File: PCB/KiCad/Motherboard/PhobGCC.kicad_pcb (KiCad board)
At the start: 2 copper layers, 125.5 x 72.9 mm, 67 parts, among them J1 Conn_01x06_Female, J2 Conn_01x04_Female, J3 Conn_01x01_Male, J5 Conn_01x02_Male, Q1 Q_NMOS_GSD, Q2 Q_PMOS_GDS, Q3 Q_NMOS_GSD, SW1 A, SW10 Dup, SW11 Dright, SW12 Ddown, SW2 B, SW3 X, SW4 Y, SW5 Start, SW6 L, SW7 R, SW8 1825027-5, SW9 Dleft, U1 Teensy4.0, U2 2x DRV5053CAQLPGM Hall Effect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, U3 GP2S60-MFG, U4 GP2S60-MFG

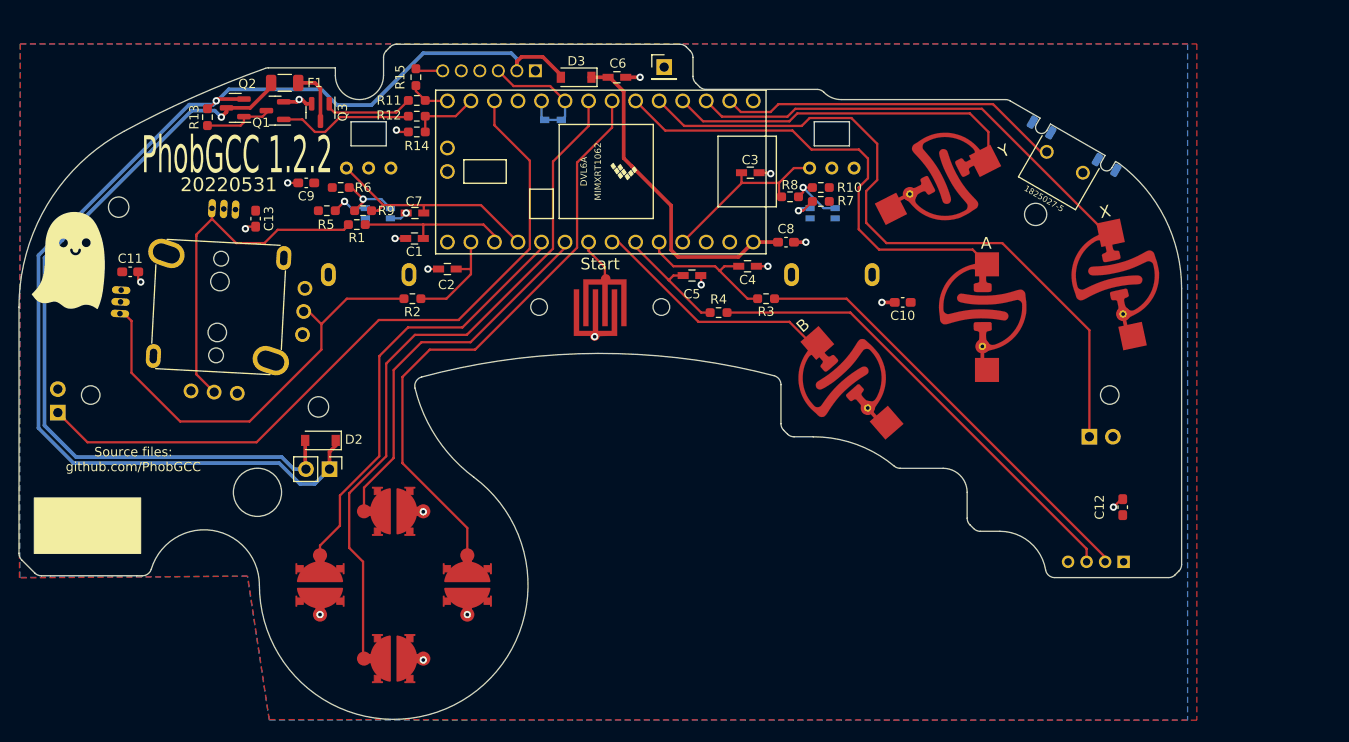
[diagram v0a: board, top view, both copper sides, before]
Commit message: Updates
- switched rumble pads to SMD and matched OEM placement.
- aligned both sets of trigger pads to be horizontal for convenience and consistency.
- centered c-stick pins to the board edge.
- rerouted some areas to have a more consistent copper fill.
- fixed trigger board width (switched 7.5mm to 7.35mm).
- increased dpad button pad size to make for easier hand soldering.
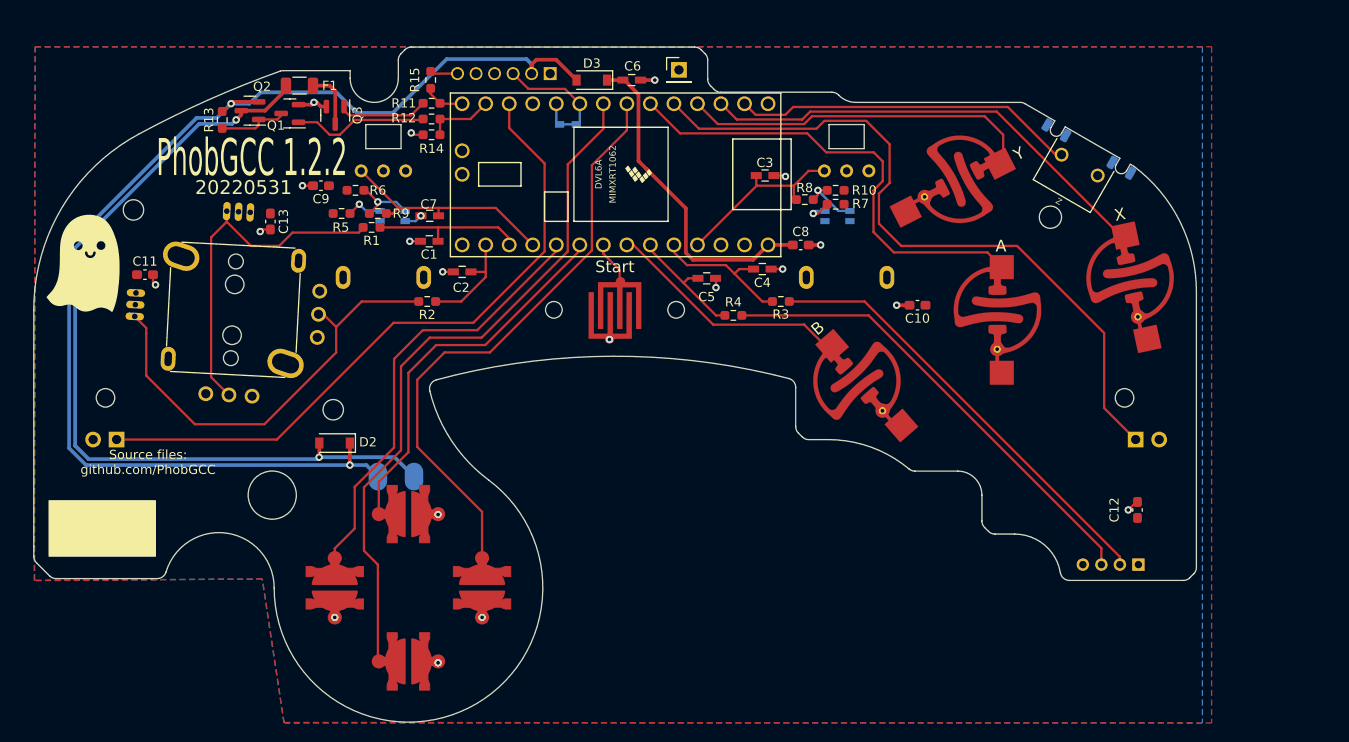
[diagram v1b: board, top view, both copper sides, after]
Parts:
- J5: moved to B.Cu
- SW8: value 1825027-5 -> Z
- moved SW6 6.98 mm to (46.5, 68.4), turned to 90 degrees
- moved J5 6.06 mm to (75.5, 72.3)
- moved SW7 5.00 mm to (156.6, 68.4)
- moved D3 1.72 mm to (97.8, 29.6)
- moved D1 1.68 mm to (95.3, 34.3), turned to 180 degrees
- moved Q2 1.62 mm to (61.0, 32.9)
- moved R13 1.62 mm to (58.0, 33.9)
- moved SW12 1.62 mm to (78.0, 92.3)
- moved C10 1.62 mm to (133.0, 53.9)
- moved C13 1.62 mm to (63.1, 44.8)
- moved C2 1.62 mm to (83.8, 50.3)
- moved C3 1.62 mm to (116.5, 39.9)
- moved C8 1.62 mm to (120.4, 47.4)
- moved H3 1.62 mm to (45.4, 63.9)
- moved H4 1.62 mm to (155.3, 63.9)
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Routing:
- net Net-(D2-Pad2): track 84.2 -> 91.1 mm, vias 1 -> 2
- net /L: track 78.5 -> 72.1 mm
- net /R: track 75.6 -> 76.9 mm
- net +5V: track 131.6 -> 131.4 mm, vias 1 -> 2
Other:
- outline, holes or cut-outs redrawn

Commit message: Consolidated footprints to PhobGCC library
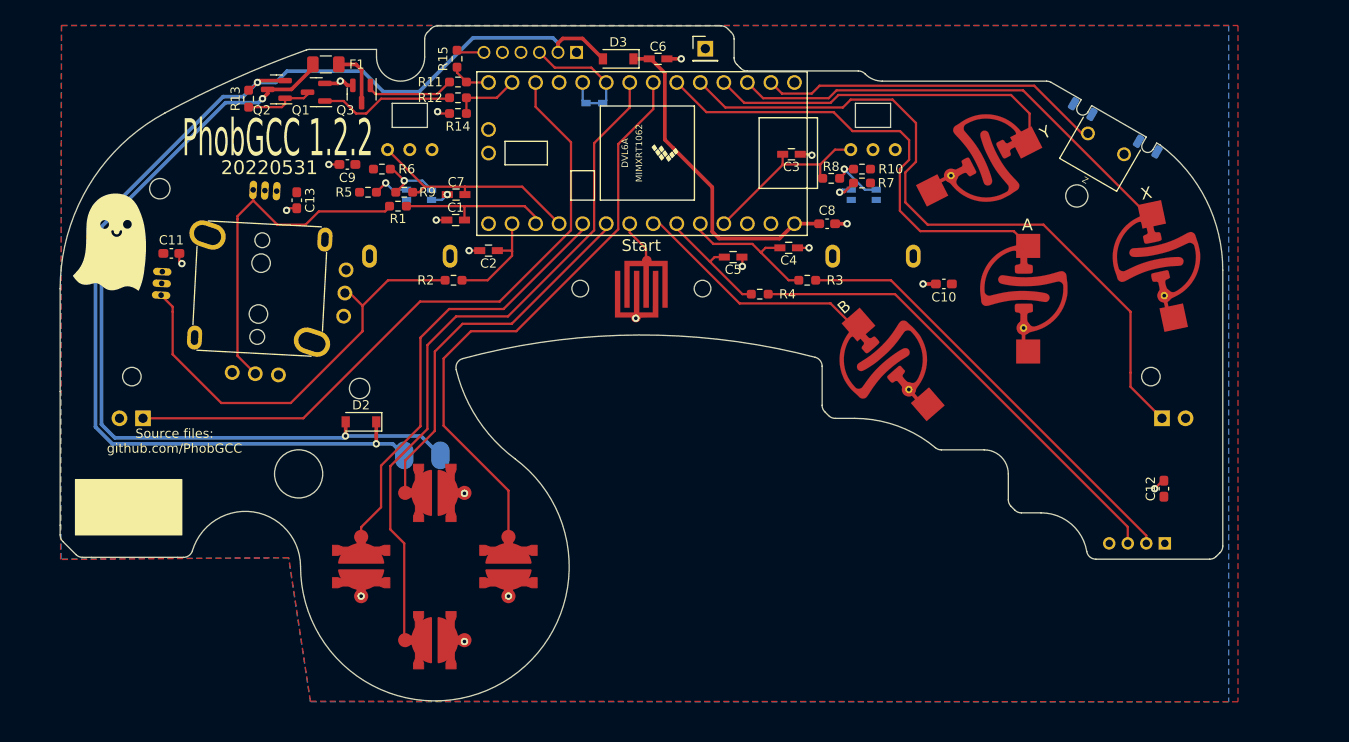
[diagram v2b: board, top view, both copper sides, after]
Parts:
- C1, C2, C3, C4, C5, C6, C7: footprint Capacitors_SMD:C_0603_HandSoldering -> PhobGCC_Footprints:C_0603_HandSoldering
- C10, C11, C12, C13, C8, C9: footprint Capacitor_SMD:C_0603_1608Metric_Pad1.08x0.95mm_HandSolder -> PhobGCC_Footprints:C_0603_1608Metric_Pad1.08x0.95mm_HandSolder
- D2, D3: footprint Diode_SMD:D_SOD-123 -> PhobGCC_Footprints:D_SOD-123
- F1: footprint Resistor_SMD:R_1206_3216Metric -> PhobGCC_Footprints:Fuse_1206_3216Metric
- J2: footprint Pin_Headers:Pin_Header_Straight_1x04_Pitch2.00mm -> PhobGCC_Footprints:PinHeader_1x04_P2.00mm_Vertical
- J3: footprint Connector_PinHeader_2.54mm:PinHeader_1x01_P2.54mm_Vertical -> PhobGCC_Footprints:PinHeader_1x01_P2.54mm_Vertical
- Q1, Q2, Q3: footprint Package_TO_SOT_SMD:SOT-23 -> PhobGCC_Footprints:SOT-23
- R1, R11, R12, R13, R14, R15, R2, R3, R4: footprint Resistor_SMD:R_0603_1608Metric_Pad0.98x0.95mm_HandSolder -> PhobGCC_Footprints:R_0603_1608Metric_Pad0.98x0.95mm_HandSolder
- R10, R5, R6, R7, R8, R9: footprint Resistor_SMD:R_0603_1608Metric_Pad0.98x0.95mm_HandSolder -> PhobGCC_Footprints:R_0603_1608_DNP
- moved C2 3.66 mm to (86.7, 48.0)
- moved RV1 3.66 mm to (78.2, 37.1)
- moved SW5 3.66 mm to (103.2, 52.1)
- moved SW9 3.66 mm to (72.9, 82.1)
- moved U3 3.66 mm to (79.2, 41.9)
- moved U4 3.66 mm to (127.2, 41.9)
- moved D3 3.66 mm to (100.7, 27.3)
- moved F1 3.66 mm to (69.1, 27.9)
- moved J1 3.66 mm to (96.2, 26.6)
- moved C7 3.66 mm to (83.2, 41.9)
- moved D1 3.66 mm to (98.1, 32.0)
- moved R10 3.66 mm to (127.0, 39.2)
- moved R7 3.66 mm to (127.0, 40.7)
- moved C13 3.66 mm to (66.0, 42.5)
- moved H1 3.66 mm to (66.2, 72.1)
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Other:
- outline, holes or cut-outs redrawn

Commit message: 1.2.3 changes
omron tactile z support, larger c stick pin holes, relocated C10 from underneath button pad
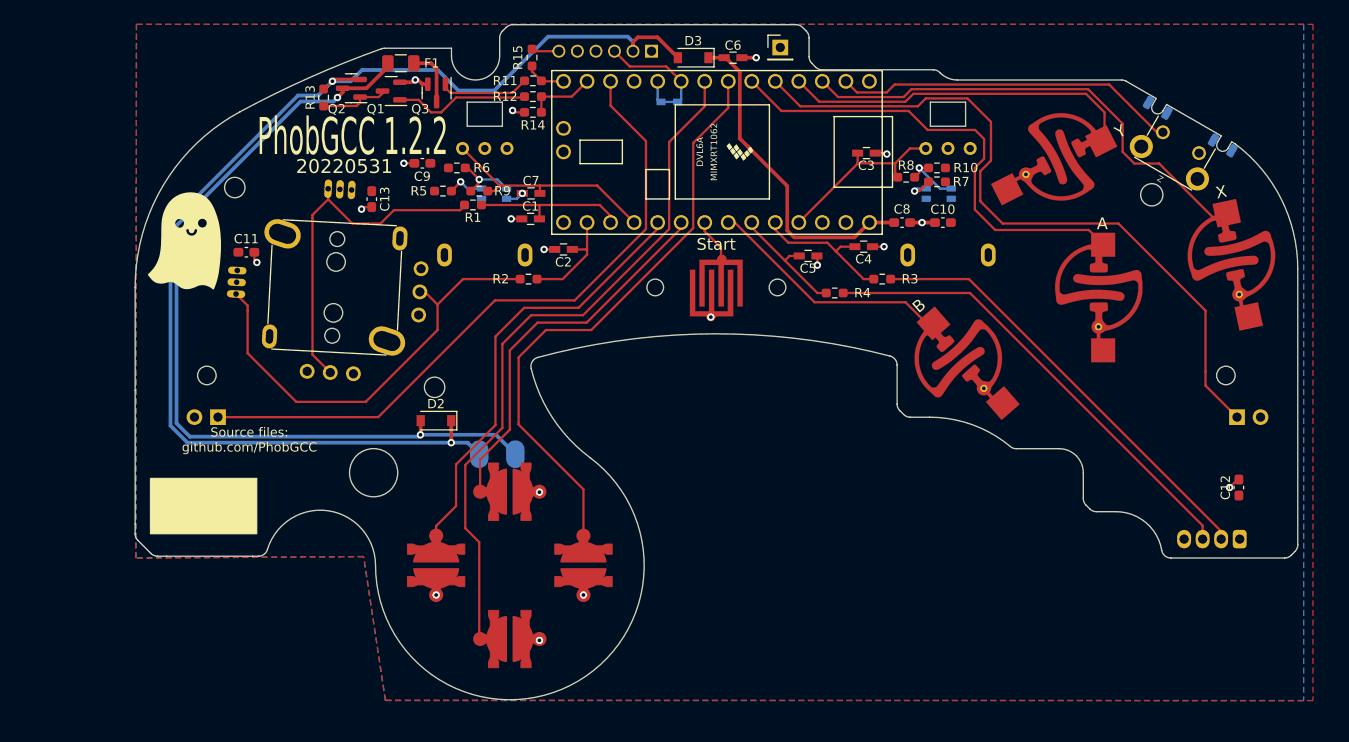
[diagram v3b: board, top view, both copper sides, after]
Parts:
- SW8: footprint PhobGCC_Footprints:Z_Switch_Edge -> PhobGCC_Footprints:Z_Switch_Edge_Omron
- moved C1 8.10 mm to (91.2, 44.5)
- moved C3 8.10 mm to (127.5, 37.4)
- moved C8 8.10 mm to (131.3, 44.9)
- moved C9 8.10 mm to (79.6, 38.5)
- moved D2 8.10 mm to (81.0, 66.3)
- moved H2 8.10 mm to (171.1, 76.9)
- moved H4 8.10 mm to (166.3, 61.4)
- moved H7 8.10 mm to (158.3, 41.9)
- moved R14 8.10 mm to (91.5, 33.0)
- moved R3 8.10 mm to (129.2, 51.0)
- moved R8 8.10 mm to (131.8, 40.0)
- moved RV2 8.10 mm to (136.3, 36.9)
- moved SW1 8.10 mm to (152.5, 51.9)
- moved SW10 8.10 mm to (89.0, 74.0)
- moved SW12 8.10 mm to (89.0, 89.9)
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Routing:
- net /X: track 50.2 -> 51.8 mm
- net GND: track 23.9 -> 24.0 mm, vias 20 -> 19

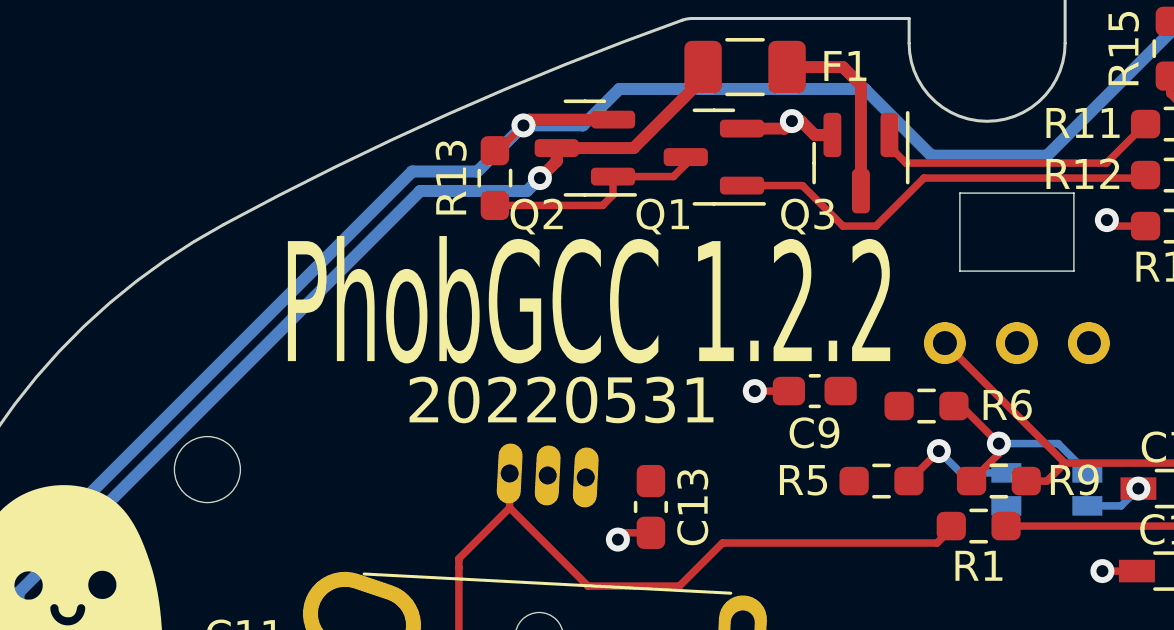
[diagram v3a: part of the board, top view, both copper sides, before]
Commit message: added back mini ghost
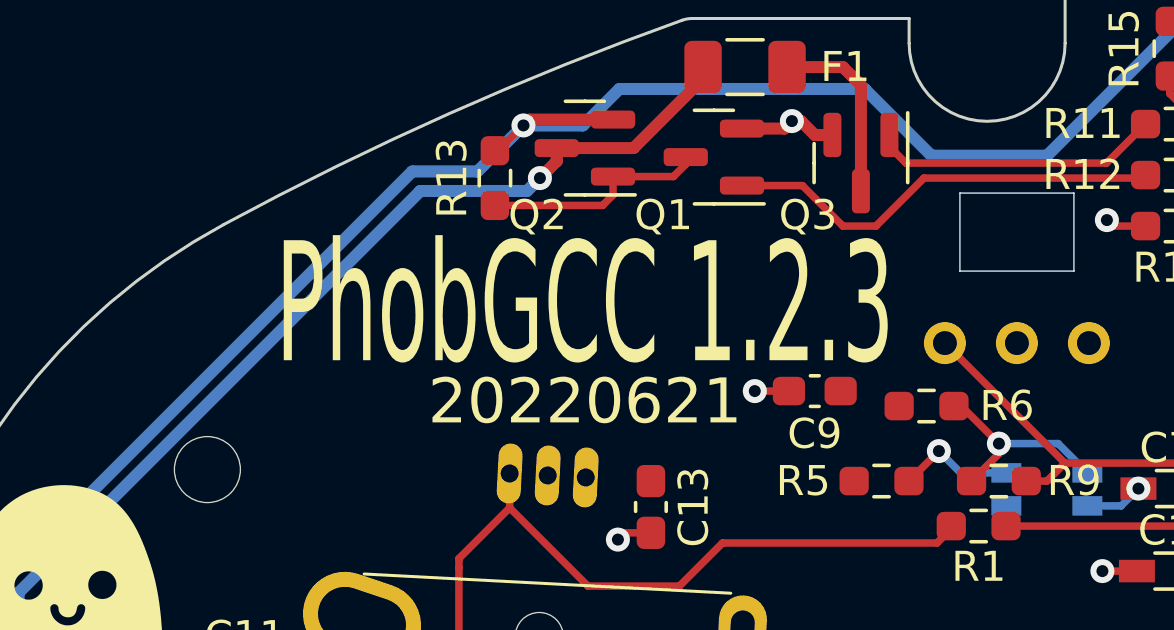
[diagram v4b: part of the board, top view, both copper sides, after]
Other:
- board text added: "20220621"
- board text added: "PhobGCC 1.2.3"
- board text removed: "20220531"
- board text removed: "PhobGCC 1.2.2"
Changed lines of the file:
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@@
   (gr_arc (start 62.827291 80.231399) (mid 62.467484 80.746508) (end 61.872 80.947) (layer "Edge.Cuts") (width 0.1))
   (gr_arc (start 75.135548 26.175395) (mid 75.301244 26.131813) (end 75.471945 26.117115) (layer "Edge.Cuts") (width 0.1))
-  (gr_text "PhobGCC 1.2.2" (at 72.032 35.687) (layer "F.SilkS")
-    (effects (font (size 4 2) (thickness 0.3)))
+  (gr_text "20220621" (at 71.895 38.887) (layer "F.SilkS")
+    (effects (font (size 1.5 1.5) (thickness 0.3)))
   )
   (gr_text "Source files:\ngithub.com/PhobGCC" (at 60.892 68.387) (layer "F.SilkS")
     (effects (font (size 1 1) (thickness 0.15)))
   )
-  (gr_text "20220531" (at 71.132 38.887) (layer "F.SilkS")
-    (effects (font (size 1.5 1.5) (thickness 0.3)))
+  (gr_text "PhobGCC 1.2.3" (at 71.895 35.657) (layer "F.SilkS")
+    (effects (font (size 4 2) (thickness 0.3)))
   )
   (segment (start 122.192 49.537) (end 122.192 48.587) (width 0.25) (layer "F.Cu") (net 1))

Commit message: attempt at v1.2.4
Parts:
- removed D1: D_Schottky_Shorted, PhobGCC_Footprints:D_SOD-523_Shorted
- removed R10, R5, R6, R7, R8, R9: DNP, PhobGCC_Footprints:R_0603_1608_DNP
- removed U3, U4: GP2S60-MFG, PhobGCC_Footprints:Sharp_Microelectronics-GP2S60-MFG
- added TSTP1: testing pads, Library:testing pads, F.Cu at (57.8, 66.3)
- added TSTP2: testing pads, Library:testing pads, F.Cu at (72.6, 54.9)
- J5: value Conn_01x02_Male -> Rumble; footprint PhobGCC_Footprints:Pin_Header_Straight_1x02_Pitch2.54mm -> PhobGCC_Footprints:rumble_pins
- moved C13 14.6 mm to (68.0, 55.7), turned to 180 degrees
- moved C11 14.1 mm to (55.3, 61.3), turned to 90 degrees
- moved C2 12.5 mm to (82.5, 50.1), turned to 90 degrees
- moved C12 11.3 mm to (156.4, 73.8)
- moved C8 11.3 mm to (120.0, 45.2)
- moved H2 11.3 mm to (159.8, 77.2)
- moved SW2 11.3 mm to (126.0, 59.8)
- moved SW3 11.3 mm to (155.5, 48.7)
- moved C6 11.3 mm to (101.8, 27.4)
- moved C7 11.3 mm to (80.0, 42.0)
- moved C9 11.3 mm to (68.3, 38.8)
- moved D2 11.3 mm to (69.7, 66.6)
- moved D3 11.3 mm to (97.5, 27.4)
- moved F1 11.3 mm to (65.9, 28.0)
- moved H1 11.3 mm to (63.0, 72.2)
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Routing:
- net /Stick_y: track 47.6 -> 14.3 mm
- net /Stick_x: track 38.1 -> 27.7 mm
- net Net-(R6-Pad2): track 6.75 -> 0.00 mm, vias 1 -> 0
- net Net-(R10-Pad2): track 6.58 -> 0.00 mm, vias 1 -> 0
- net Net-(R5-Pad2): track 3.96 -> 0.00 mm, vias 1 -> 0
- net /Data: track 15.0 -> 11.1 mm
- net +3V3: track 0.00 -> 3.59 mm, vias 0 -> 2
- net Net-(R7-Pad2): track 3.28 -> 0.00 mm, vias 1 -> 0
- net /Stick_x_filt: track 16.7 -> 14.0 mm
- net /Ranalog: track 19.4 -> 17.0 mm
- net GND: track 24.0 -> 26.0 mm
- net /Stick_y_filt: track 11.7 -> 9.83 mm
- net /L: track 72.1 -> 73.7 mm
- net /Lanalog: track 24.2 -> 22.7 mm
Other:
- outline, holes or cut-outs redrawn
- board text added: "20221007"
- board text added: "PhobGCC 1.2.4"
- board text removed: "20220621"
- board text removed: "PhobGCC 1.2.3"
